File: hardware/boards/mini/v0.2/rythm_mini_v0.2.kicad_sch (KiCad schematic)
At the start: 84 parts, among them IC1 NAU88C22YG, IC2 IS42S32160F-6BLI, Q1 PMV37EN22, U1 W25Q128JVP, U2 LTV-217-G, U3 RythmMini, U4 STM32H750XBHx, U5 MT48LC32M8A2TG, Y1 Crystal_GND24

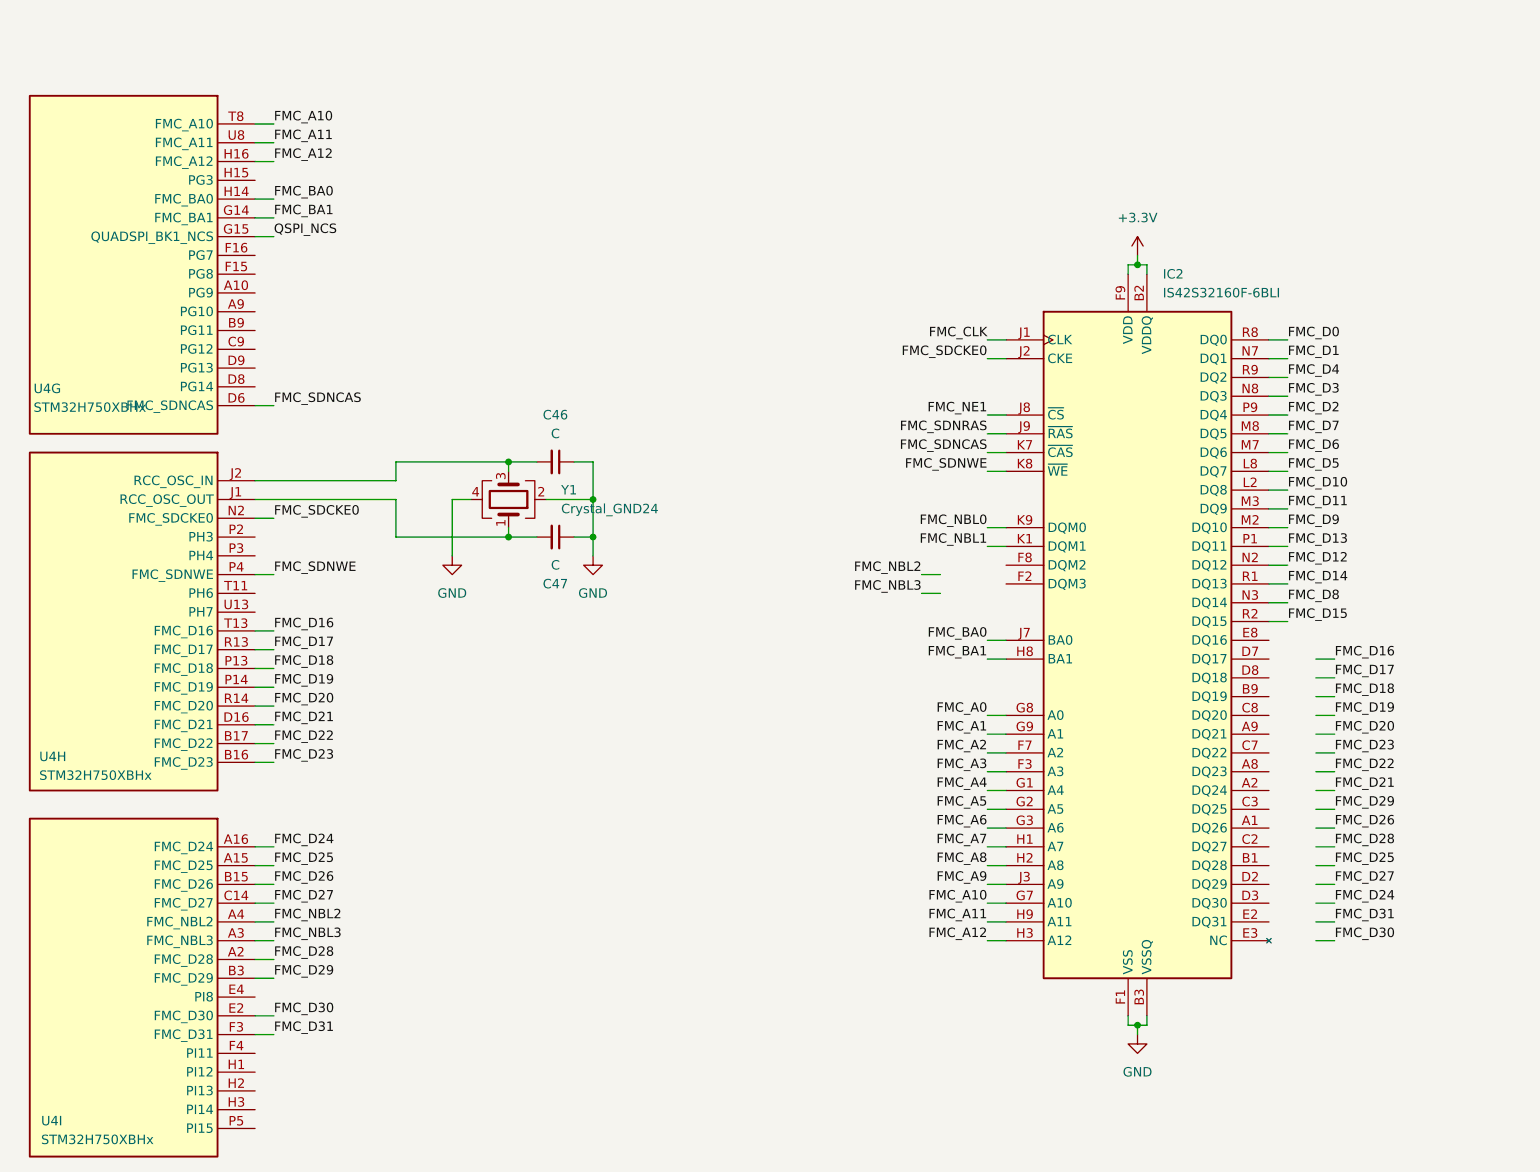
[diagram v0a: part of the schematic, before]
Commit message: mini: change to x16 SDRAM
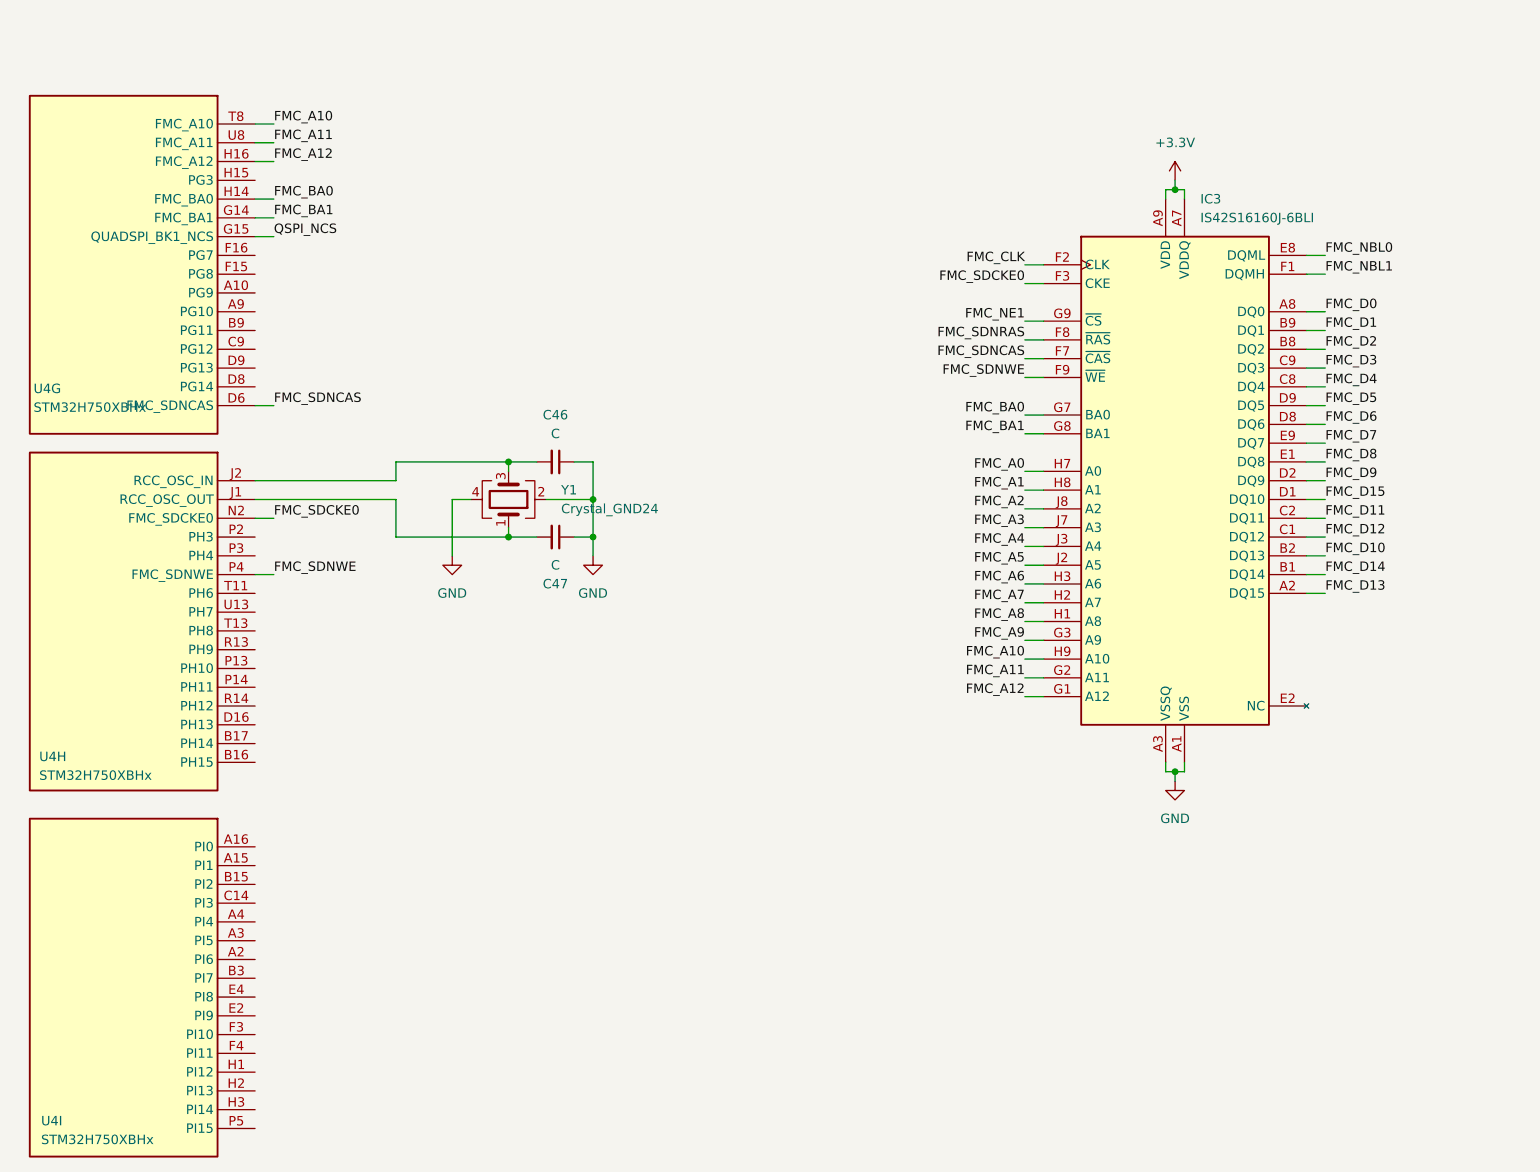
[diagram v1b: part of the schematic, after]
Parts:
- removed IC2: IS42S32160F-6BLI, Package_BGA:BGA-90_8.0x13.0mm_Layout2x3x15_P0.8mm, symbol IS42S32160F-6BLI:IS42S32160F-6BLI
- added IC3: IS42S16160J-6BLI, Package_BGA:Alliance_TFBGA-54_8x8mm_Layout9x9_P0.8mm, symbol IS42S16160J-6BLI:IS42S16160J-6BLI
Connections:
- net +3.3V: now also IC3.A7 (VDDQ), IC3.A9 (VDD), IC3.B3 (VDDQ), IC3.C7 (VDDQ), IC3.D3 (VDDQ), IC3.E7 (VDD), IC3.J9 (VDD)
- net FMC_A0: now also IC3.H7 (A0)
- net FMC_A1: now also IC3.H8 (A1)
- net FMC_A10: now also IC3.H9 (A10)
- net FMC_A11: now also IC3.G2 (A11)
- net FMC_A12: now also IC3.G1 (A12)
- net FMC_A2: now also IC3.J8 (A2)
- net FMC_A3: now also IC3.J7 (A3)
- net FMC_A4: now also IC3.J3 (A4)
- net FMC_A5: now also IC3.J2 (A5)
- net FMC_A6: now also IC3.H3 (A6)
- net FMC_A7: now also IC3.H2 (A7)
- net FMC_A8: now also IC3.H1 (A8)
- net FMC_A9: now also IC3.G3 (A9)
- net FMC_BA0: now also IC3.G7 (BA0)
- net FMC_BA1: now also IC3.G8 (BA1)
- net FMC_CLK: now also IC3.F2 (CLK)
- net FMC_D0: now also IC3.A8 (DQ0)
- net FMC_D1: now also IC3.B9 (DQ1)
- net FMC_D10: now also IC3.B2 (DQ13)
- net FMC_D11: now also IC3.C2 (DQ11)
- net FMC_D12: now also IC3.C1 (DQ12)
- net FMC_D13: now also IC3.A2 (DQ15)
- net FMC_D14: now also IC3.B1 (DQ14)
- net FMC_D15: now also IC3.D1 (DQ10)
- net FMC_D2: now also IC3.B8 (DQ2)
- net FMC_D3: now also IC3.C9 (DQ3)
- net FMC_D4: now also IC3.C8 (DQ4)
- net FMC_D5: now also IC3.D9 (DQ5)
- net FMC_D6: now also IC3.D8 (DQ6)
- net FMC_D7: now also IC3.E9 (DQ7)
- net FMC_D8: now also IC3.E1 (DQ8)
- net FMC_D9: now also IC3.D2 (DQ9)
- net FMC_NBL0: now also IC3.E8 (DQML)
- net FMC_NBL1: now also IC3.F1 (DQMH)
- net FMC_NE1: now also IC3.G9 (~{CS})
- net FMC_SDCKE0: now also IC3.F3 (CKE)
- net FMC_SDNCAS: now also IC3.F7 (~{CAS})
- net FMC_SDNRAS: now also IC3.F8 (~{RAS})
- net FMC_SDNWE: now also IC3.F9 (~{WE})
- net GND: now also IC3.A1 (VSS), IC3.A3 (VSSQ), IC3.B7 (VSSQ), IC3.C3 (VSSQ), IC3.D7 (VSSQ), IC3.E3 (VSS), IC3.J1 (VSS)
- net FMC_D16: no longer names the net of U4.T13 (PH8)
- net FMC_D17: no longer names the net of U4.R13 (PH9)
- net FMC_D18: no longer names the net of U4.P13 (PH10)
- net FMC_D19: no longer names the net of U4.P14 (PH11)
- net FMC_D20: no longer names the net of U4.R14 (PH12)
- net FMC_D21: no longer names the net of U4.D16 (PH13)
- net FMC_D22: no longer names the net of U4.B17 (PH14)
- net FMC_D23: no longer names the net of U4.B16 (PH15)
- net FMC_D24: no longer names the net of U4.A16 (PI0)
- net FMC_D25: no longer names the net of U4.A15 (PI1)
- net FMC_D26: no longer names the net of U4.B15 (PI2)
- net FMC_D27: no longer names the net of U4.C14 (PI3)
- net FMC_D28: no longer names the net of U4.A2 (PI6)
- net FMC_D29: no longer names the net of U4.B3 (PI7)
- net FMC_D30: no longer names the net of U4.E2 (PI9)
- net FMC_D31: no longer names the net of U4.F3 (PI10)
- net FMC_NBL2: no longer names the net of U4.A4 (PI4)
- net FMC_NBL3: no longer names the net of U4.A3 (PI5)

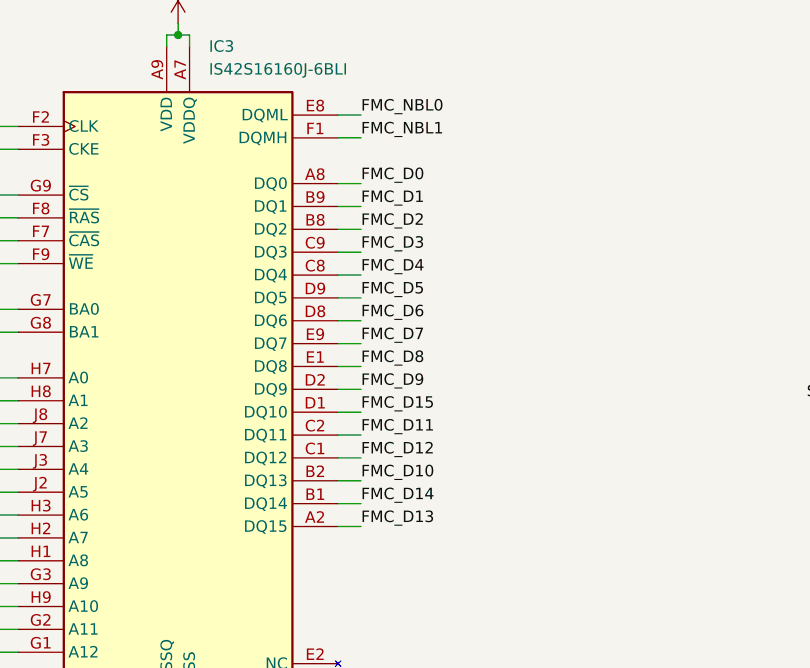
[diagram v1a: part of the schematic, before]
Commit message: mini: routed x16 SDRAM
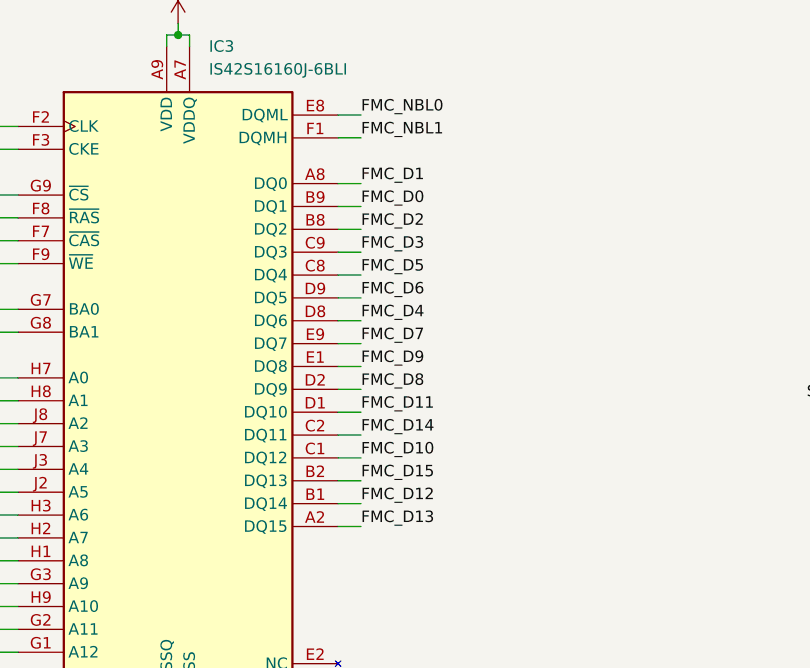
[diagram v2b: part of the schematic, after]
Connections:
- net FMC_D0: now also IC3.B9 (DQ1); no longer IC3.A8 (DQ0)
- net FMC_D1: now also IC3.A8 (DQ0); no longer IC3.B9 (DQ1)
- net FMC_D10: now also IC3.C1 (DQ12); no longer IC3.B2 (DQ13)
- net FMC_D11: now also IC3.D1 (DQ10); no longer IC3.C2 (DQ11)
- net FMC_D12: now also IC3.B1 (DQ14); no longer IC3.C1 (DQ12)
- net FMC_D14: now also IC3.C2 (DQ11); no longer IC3.B1 (DQ14)
- net FMC_D15: now also IC3.B2 (DQ13); no longer IC3.D1 (DQ10)
- net FMC_D4: now also IC3.D8 (DQ6); no longer IC3.C8 (DQ4)
- net FMC_D5: now also IC3.C8 (DQ4); no longer IC3.D9 (DQ5)
- net FMC_D6: now also IC3.D9 (DQ5); no longer IC3.D8 (DQ6)
- net FMC_D8: now also IC3.D2 (DQ9); no longer IC3.E1 (DQ8)
- net FMC_D9: now also IC3.E1 (DQ8); no longer IC3.D2 (DQ9)
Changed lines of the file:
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@@
 	)
 	(label "FMC_D8"
-		(at 154.94 257.81 0)
+		(at 154.94 260.35 0)
 		(effects
 			(font
@@
 	)
 	(label "FMC_D11"
-		(at 154.94 265.43 0)
+		(at 154.94 262.89 0)
 		(effects
 			(font
@@
 	)
 	(label "FMC_D0"
-		(at 154.94 237.49 0)
+		(at 154.94 240.03 0)
 		(effects
 			(font
@@
 	)
 	(label "FMC_D15"
-		(at 154.94 262.89 0)
+		(at 154.94 270.51 0)
 		(effects
 			(font
@@
 	)
 	(label "FMC_D5"
-		(at 154.94 250.19 0)
+		(at 154.94 247.65 0)
 		(effects
 			(font
@@
 	)
 	(label "FMC_D4"
-		(at 154.94 247.65 0)
+		(at 154.94 252.73 0)
 		(effects
 			(font
@@
 	)
 	(label "FMC_D9"
-		(at 154.94 260.35 0)
+		(at 154.94 257.81 0)
 		(effects
 			(font
@@
 	)
 	(label "FMC_D1"
-		(at 154.94 240.03 0)
+		(at 154.94 237.49 0)
 		(effects
 			(font
@@
 	)
 	(label "FMC_D14"
-		(at 154.94 273.05 0)
+		(at 154.94 265.43 0)
 		(effects
 			(font
@@
 	)
 	(label "FMC_D12"
-		(at 154.94 267.97 0)
+		(at 154.94 273.05 0)
 		(effects
 			(font
@@
 	)
 	(label "FMC_D10"
-		(at 154.94 270.51 0)
+		(at 154.94 267.97 0)
 		(effects
 			(font
@@
 	)
 	(label "FMC_D6"
-		(at 154.94 252.73 0)
-		(effects
-			(font
+		(at 154.94 250.19 0)
+		(effects
+			(font
